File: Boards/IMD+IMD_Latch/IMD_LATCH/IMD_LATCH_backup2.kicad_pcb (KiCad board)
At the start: 2 copper layers, 50 x 25 mm, 33 parts, among them J1 UF_5_VT, J2 MM_F_RA_04, J3 MicroFit_V_2, K1 G5Q-1A4-DC5-5V, Q1 SSM3K333R, Q2 SSM3K333R, U1 TLV3701QDBVRG4Q1, U2 CD4043BPWR, U3 TLV3701QDBVRG4Q1

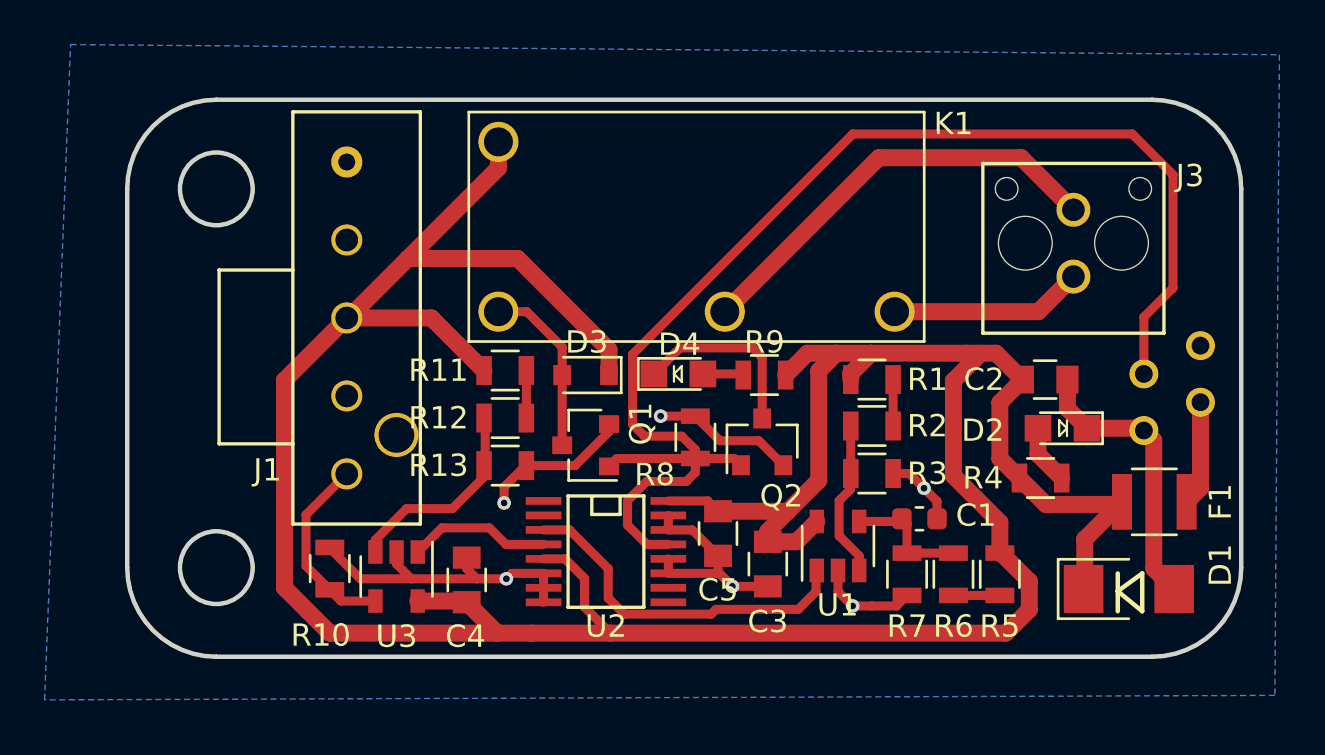
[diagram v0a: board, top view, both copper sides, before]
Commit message: Layout revision with updated connector placement and back layer.
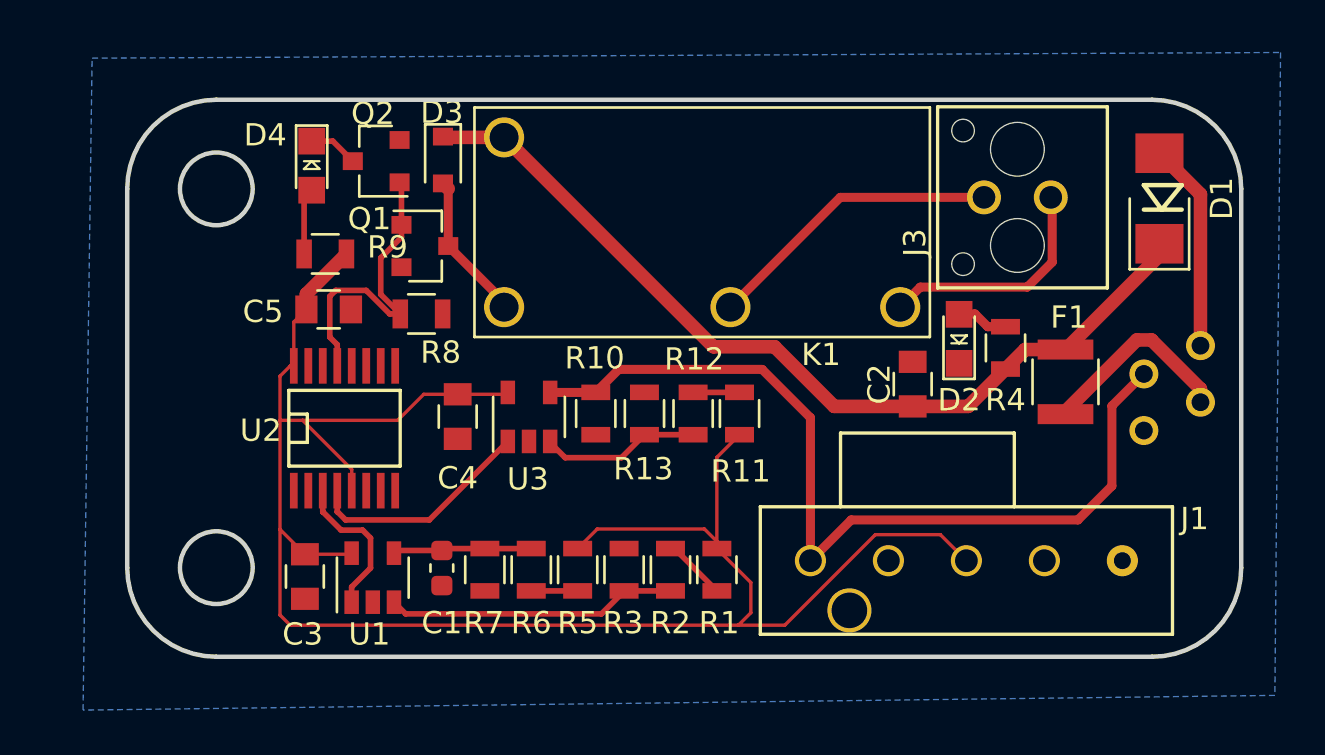
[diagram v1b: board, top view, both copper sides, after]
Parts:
- moved J1 27.6 mm to (224.9, 117.8), turned to 270 degrees
- moved C1 21.6 mm to (203.1, 118.1), turned to 270 degrees
- moved Q2 21.4 mm to (200.2, 99.9), turned to 180 degrees
- moved U1 20.9 mm to (200.1, 118.6)
- moved C3 20.8 mm to (197.0, 118.5)
- moved R9 20.4 mm to (197.9, 104.0)
- moved C5 20.2 mm to (198.1, 106.5), turned to 180 degrees
- moved R6 18.9 mm to (207.2, 118.2)
- moved R5 18.9 mm to (209.2, 118.2)
- moved R7 18.9 mm to (205.1, 118.2)
- moved D4 18.9 mm to (197.3, 100.1), turned to 270 degrees
- moved D1 17.6 mm to (235.4, 101.5), turned to 90 degrees
- moved R10 13.8 mm to (210.1, 111.2), turned to 270 degrees
- moved R8 13.5 mm to (202.2, 106.7), turned to 0 degrees
- moved U2 13.0 mm to (198.8, 111.9), turned to 0 degrees
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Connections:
- J2 pad 3: /IMD_Status_Output -> /IMD_Output
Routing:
- net GND: track 58.4 -> 9.40 mm, vias 6 -> 0
- net /IMD_Status_Output: track 59.3 -> 13.7 mm
- net /IMD_Output: track 8.66 -> 40.2 mm
- net /12V_Fused: track 146.5 -> 126.7 mm
- net Net-(U1-Pad1): track 15.9 -> 6.81 mm
- net Net-(J3-Pad2): track 19.5 -> 13.4 mm
- net Net-(D4-Pad1): track 8.26 -> 2.22 mm
- net Net-(R2-Pad1): track 7.46 -> 13.1 mm
- net +12V: track 4.73 -> 9.02 mm
- net Net-(U2-Pad4): track 6.40 -> 10.2 mm
- net Net-(J3-Pad1): track 8.68 -> 10.6 mm
- net Net-(R12-Pad1): track 8.80 -> 7.18 mm
- net Net-(D3-Pad2): track 7.93 -> 6.69 mm
- net Net-(D4-Pad2): track 1.83 -> 3.00 mm
- net Net-(R1-Pad1): track 2.08 -> 2.87 mm
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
